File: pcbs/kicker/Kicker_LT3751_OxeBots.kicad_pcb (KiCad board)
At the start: 2 copper layers, 117.9 x 140 mm, 91 parts, among them J1 XT30PW-F, J2 Conn_01x02, J3 Conn_01x02, J4 Conn_01x08, J5 XT30PW-F, Q1 BC847, Q2 BC847, Q3 IRFB4227, Q4 TIC106, Q5 FQPF20N60, T1 DCT15EFD-U44S003, U1 LM324, U2 LMV358, U3 TLV431DBZ, U4 LT3751, U5 AQV454, U6 HCNR201, U7 HCPL-3120, U8 LM358

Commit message: Desenhada versão inicial da PCB.
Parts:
- removed C6: 100nF, Capacitor_SMD:C_0805_2012Metric_Pad1.18x1.45mm_HandSolder
- removed R13, R8, R9: 10k, Resistor_SMD:R_0805_2012Metric_Pad1.20x1.40mm_HandSolder
- removed R27: 5.6k, Resistor_SMD:R_0805_2012Metric_Pad1.20x1.40mm_HandSolder
- removed R28, R5: 1k, Resistor_SMD:R_0805_2012Metric_Pad1.20x1.40mm_HandSolder
- removed U2: LMV358, Package_SO:SOIC-8_5.3x6.2mm_P1.27mm
- C8: footprint Capacitor_THT:C_Disc_D5.0mm_W2.5mm_P2.50mm -> Capacitor_SMD:C_0805_2012Metric_Pad1.18x1.45mm_HandSolder
- D4, R7: moved to B.Cu
- R34: footprint Resistor_THT:R_Axial_DIN0207_L6.3mm_D2.5mm_P7.62mm_Horizontal -> Resistor_THT:R_Axial_DIN0207_L6.3mm_D2.5mm_P15.24mm_Horizontal
- R42: footprint Resistor_THT:R_Axial_DIN0207_L6.3mm_D2.5mm_P15.24mm_Horizontal -> Resistor_THT:R_Axial_DIN0207_L6.3mm_D2.5mm_P7.62mm_Horizontal
- moved R22 19.8 mm to (78.3, 64.0), turned to 135 degrees
- moved R17 18.4 mm to (79.2, 68.1), turned to -135 degrees
- moved R21 18.2 mm to (72.8, 70.2), turned to 135 degrees
- moved F1 16.1 mm to (72.1, 100.7), turned to -90 degrees
- moved Q2 13.9 mm to (75.4, 66.9), turned to 135 degrees
- moved R16 13.7 mm to (73.8, 74.0), turned to -135 degrees
- moved C3 13.3 mm to (81.2, 88.0), turned to -90 degrees
- moved D4 12.8 mm to (79.3, 112.1), turned to 0 degrees
- moved R42 12.7 mm to (132.7, 61.0)
- moved R11 9.81 mm to (46.6, 124.9), turned to 0 degrees
- moved R12 9.81 mm to (64.5, 77.6), turned to -90 degrees
- moved Q1 9.29 mm to (69.6, 72.7), turned to 135 degrees
- moved R34 9.04 mm to (119.3, 134.1), turned to 90 degrees
- moved R37 7.64 mm to (117.9, 143.4), turned to 180 degrees
- moved R24 6.97 mm to (56.8, 108.0), turned to 180 degrees
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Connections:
- C9 pad 1: Net-(U1C--) -> Net-(U1D--)
- C9 pad 2: Net-(U1B-+) -> Net-(U1C-+)
- J4 pad 3: EXT_OUT_FB -> EXT_OUT_LT3751_FAULT
- J4 pad 4: EXT_OUT_LT3751_FAULT -> EXT_OUT_LT3751_DONE
- J4 pad 5: EXT_OUT_LT3751_DONE -> EXT_OUT_FB
- R12 pad 1: Net-(U2A-+) -> EXT_OUT_FB
- R12 pad 2: Net-(U1D--) -> Net-(U1A--)
- R14 pad 2: Net-(U1A--) -> Net-(U1B--)
- R23 pad 1: Net-(U1B--) -> Net-(U1C--)
- R23 pad 2: Net-(U1A-+) -> Net-(U1B-+)
- R25 pad 1: Net-(U1B--) -> Net-(U1C--)
- R25 pad 2: Net-(U1D-+) -> Net-(U1A-+)
- R26 pad 1: Net-(U1D-+) -> Net-(U1A-+)
- R31 pad 2: Net-(U1C--) -> Net-(U1D--)
- R41 pad 1: Net-(U8A--) -> Net-(U8B--)
- R41 pad 2: Net-(U8B--) -> Net-(U8A--)
- R44 pad 2: Net-(U8B-+) -> Net-(U8A-+)
- R45 pad 1: Net-(U8B-+) -> Net-(U8A-+)
- RV1 pad 1: Net-(U1A-+) -> Net-(U1B-+)
- RV2 pad 2: Net-(U1B-+) -> Net-(U1C-+)
- RV2 pad 3: Net-(U1B-+) -> Net-(U1C-+)
- U1 pad 10: GND -> Net-(U1C-+)
- U1 pad 12: Net-(U1D-+) -> GND
- U1 pad 14: Net-(U1D--) -> Net-(U1C-+)
- U1 pad 8: Net-(U1B-+) -> Net-(U1C--)
- U6 pad 3: Net-(U8A--) -> Net-(U8B--)
- U6 pad 6: Net-(U1C--) -> Net-(U1D--)
- U8 pad 1: Net-(R36-Pad2) -> Net-(U8A--)
- U8 pad 3: GNDPWR -> Net-(U8A-+)
- U8 pad 5: Net-(U8B-+) -> GNDPWR
- U8 pad 7: Net-(U8B--) -> Net-(R36-Pad2)
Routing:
- net +12V: track 33.7 -> 175.0 mm, vias 0 -> 3
- net EXT_IN_LT3751_ENABLE: track 1.21 -> 53.8 mm
- net Net-(U1D--): track 15.0 -> 61.4 mm
- net LT3751_FAULT: track 48.2 -> 84.1 mm, vias 0 -> 1
- net Net-(Q3-G): track 0.00 -> 29.0 mm
- net LT3751_DONE: track 49.3 -> 75.8 mm, vias 0 -> 1
- net Net-(U1C-+): track 0.00 -> 22.2 mm, vias 0 -> 2
- net Net-(U1A--): track 7.87 -> 29.9 mm, vias 1 -> 2
- net EXT_IN_LT3751_KICK_1: track 13.5 -> 34.6 mm
- net GNDPWR: track 20.7 -> 0.00 mm, vias 0 -> 37
- net Net-(R5-Pad2): track 19.9 -> 0.00 mm
- net Net-(Q3-S): track 0.08 -> 18.5 mm, vias 0 -> 2
- net Net-(U8A-+): track 0.00 -> 18.4 mm
- net Net-(U2A-+): track 18.1 -> 0.00 mm, vias 2 -> 0
- net Net-(Q3-D): track 0.03 -> 17.0 mm
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- added copper zone on B.Cu, net +24V
- added copper zone on F.Cu, net +24V
- added copper zone on B.Cu, net GND
- added copper zone on F.Cu, net GND
- added copper zone on B.Cu, net Net-(F1-Pad1)

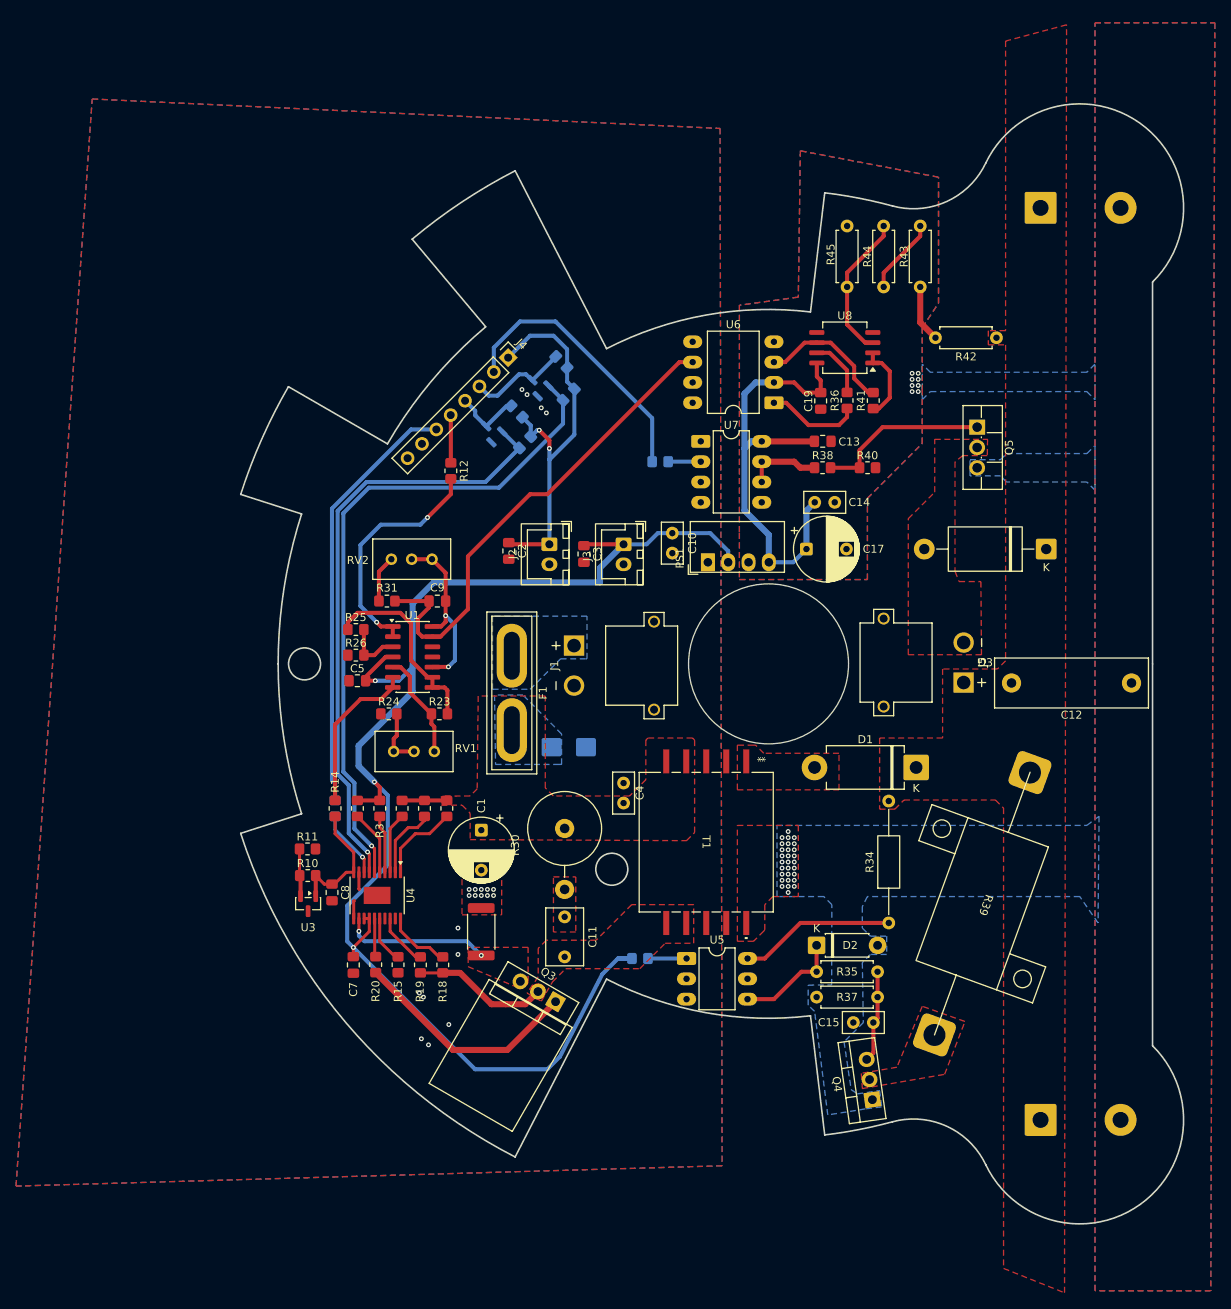
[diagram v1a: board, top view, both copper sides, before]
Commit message: Revisados os furos e adicionado MCU STM32
* Adicionado MCU STM32
* Corrigida posição dos furos
* Invertida a posição dos capacitores
* Realizadas melhorias na em geral
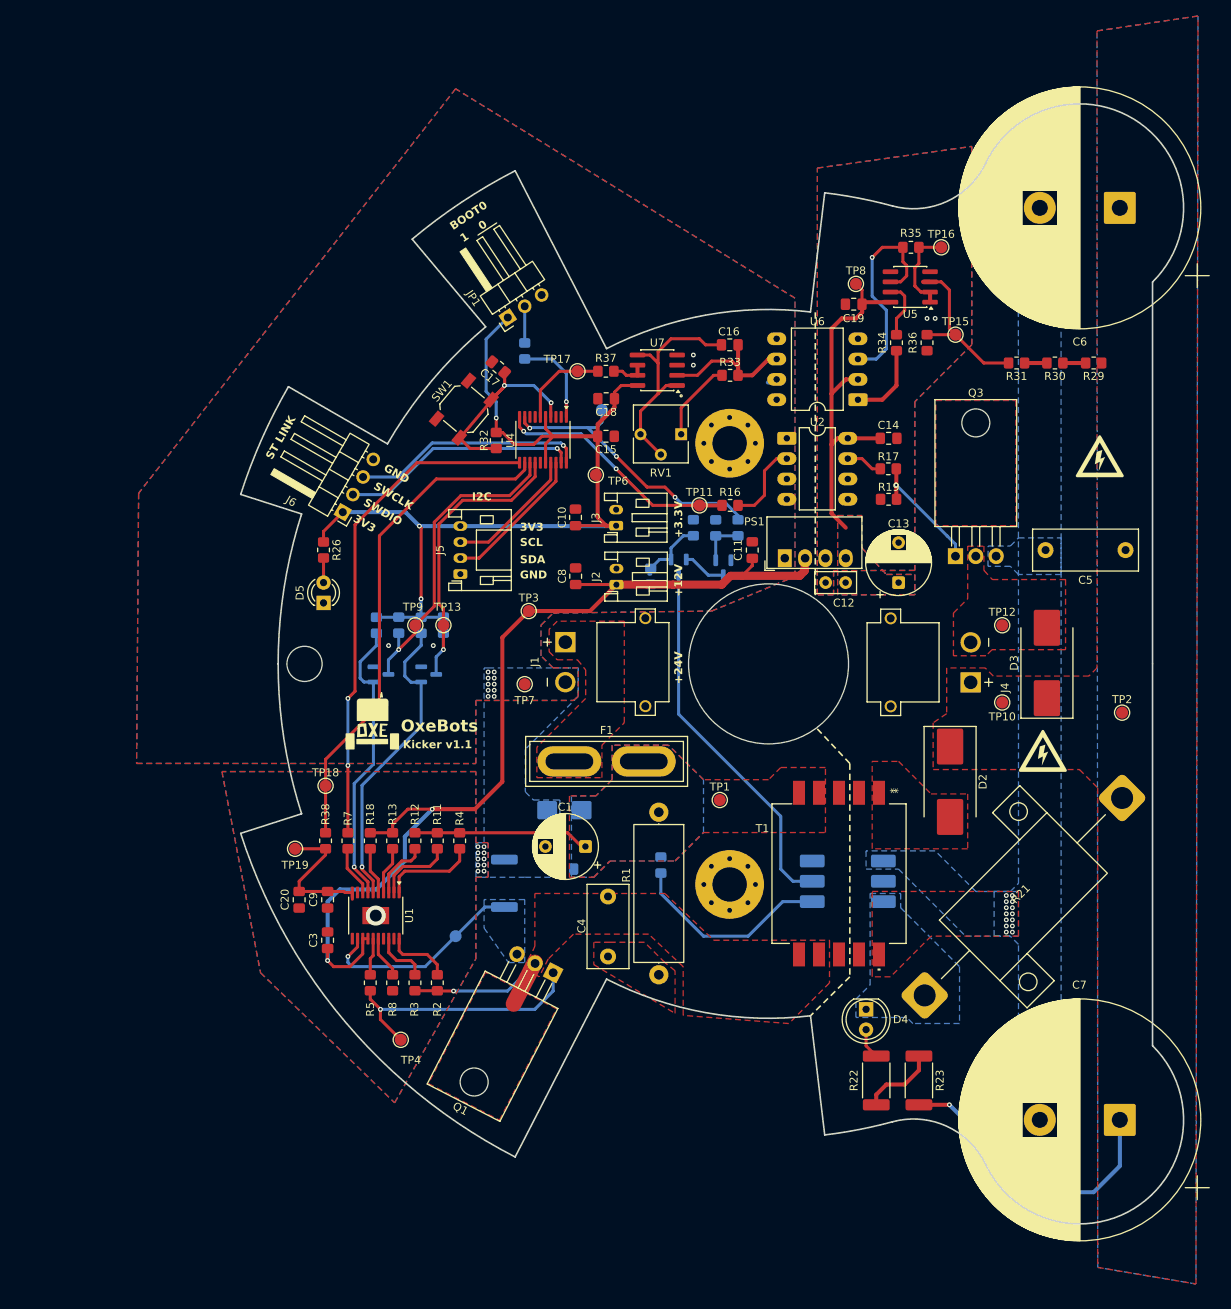
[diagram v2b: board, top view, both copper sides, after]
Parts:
- removed the C11 at (78.7, 133.3)
- removed the C5 at (52.8, 103.8)
- removed the C8 at (49.7, 130.3)
- removed the D1 at (122.7, 114.7)
- removed the J4 at (71.7, 63.4)
- removed the Q1 at (69.6, 72.7)
- removed the R11 at (46.6, 124.9)
- removed the R12 at (64.5, 77.6)
- removed the R16 at (73.8, 74.0)
- removed the R17 at (79.2, 68.1)
- removed the R31 at (56.5, 93.9)
- removed the R34 at (119.3, 134.1)
- removed the R35 at (110.2, 140.2)
- removed RV2: 100k, Potentiometer_THT:Potentiometer_Bourns_3296W_Vertical
- removed the U1 at (59.7, 100.9)
- removed the U3 at (46.7, 131.7)
- added C16: 1nF, Capacitor_SMD:C_0805_2012Metric_Pad1.18x1.45mm_HandSolder, F.Cu at (99.4, 61.8)
- added C17: 100nF, Capacitor_SMD:C_0805_2012Metric_Pad1.18x1.45mm_HandSolder, F.Cu at (70.4, 64.6)
- added C18: 100nF, Capacitor_SMD:C_0805_2012Metric_Pad1.18x1.45mm_HandSolder, F.Cu at (83.9, 68.6)
- added C20: 100nF, Capacitor_SMD:C_0805_2012Metric_Pad1.18x1.45mm_HandSolder, F.Cu at (45.6, 131.2)
- added C4: 2.2nF, Capacitor_THT:C_Rect_L10.3mm_W5.0mm_P7.50mm_MKS4, F.Cu at (84.2, 138.3)
- added D4: LED, LED_THT:LED_D5.0mm, F.Cu at (116.4, 144.9)
- added D5: LED, LED_THT:LED_D3.0mm, F.Cu at (48.6, 94.1)
- added G***: LOGO, oxebots:Logo_OxeBots_10mm, F.Cu at (54.6, 109.3)
- added G***: LOGO, oxebots:Icon_High_Voltage_10mm, F.Cu at (145.6, 76.1)
- added G***: LOGO, oxebots:Icon_High_Voltage_10mm, F.Cu at (138.5, 112.9)
- added G***: LOGO, oxebots:Icon_High_Voltage_10mm, B.Cu at (124.8, 114.9)
- added H1: MountingHole, MountingHole:MountingHole_4.3mm_M4_Pad_Via, F.Cu at (99.4, 74.2)
- added H2: MountingHole, MountingHole:MountingHole_4.3mm_M4_Pad_Via, F.Cu at (99.4, 129.3)
- added J5: I2C, Connector_JST:JST_PH_S4B-PH-K_1x04_P2.00mm_Horizontal, F.Cu at (65.7, 90.5)
- added J6: ST Link, Connector_PinHeader_2.54mm:PinHeader_1x04_P2.54mm_Horizontal, F.Cu at (51.0, 82.8)
- added JP1: Boot0, Connector_PinHeader_2.54mm:PinHeader_1x03_P2.54mm_Horizontal, F.Cu at (71.6, 58.4)
- added Q5: BSS138, Package_TO_SOT_SMD:SOT-23, B.Cu at (93.0, 89.6)
- added Q6: BSS138, Package_TO_SOT_SMD:SOT-23, B.Cu at (98.6, 89.7)
- added R15: 1k, Resistor_SMD:R_0805_2012Metric_Pad1.20x1.40mm_HandSolder, B.Cu at (63.6, 96.9)
- added R27: 10R, Resistor_SMD:R_0805_2012Metric_Pad1.20x1.40mm_HandSolder, B.Cu at (100.4, 84.7)
- added R28: 10k, Resistor_SMD:R_0805_2012Metric_Pad1.20x1.40mm_HandSolder, B.Cu at (97.6, 84.7)
- added R32: 10k, Resistor_SMD:R_0805_2012Metric_Pad1.20x1.40mm_HandSolder, F.Cu at (70.2, 73.8)
- added R33: 47k, Resistor_SMD:R_0805_2012Metric_Pad1.20x1.40mm_HandSolder, F.Cu at (99.4, 65.7)
- added R38: 10k, Resistor_SMD:R_0805_2012Metric_Pad1.20x1.40mm_HandSolder, F.Cu at (48.9, 123.8)
- added R9: 10k, Resistor_SMD:R_0805_2012Metric_Pad1.20x1.40mm_HandSolder, B.Cu at (55.2, 96.9)
- added SW1: SW_Push, Button_Switch_SMD:SW_SPST_SKQG_WithStem, F.Cu at (66.1, 69.9)
- added TP1: +24V, TestPoint:TestPoint_Pad_D1.5mm, F.Cu at (98.1, 118.7)
- added TP10: SOL+, TestPoint:TestPoint_Pad_D1.5mm, F.Cu at (133.4, 106.6)
- added TP11: KICK_PWM, TestPoint:TestPoint_Pad_D1.5mm, F.Cu at (95.6, 81.9)
- added TP12: SOL-, TestPoint:TestPoint_Pad_D1.5mm, F.Cu at (133.4, 96.9)
- added TP13: FAULT, TestPoint:TestPoint_Pad_D1.5mm, F.Cu at (63.6, 96.9)
- added TP14: BLEEDER, TestPoint:TestPoint_Pad_D1.5mm, B.Cu at (83.4, 70.0)
- added TP15: VD_SEC, TestPoint:TestPoint_Pad_D1.5mm, F.Cu at (127.6, 60.6)
- added TP16: VD_SEC_BUFFER, TestPoint:TestPoint_Pad_D1.5mm, F.Cu at (125.8, 49.7)
- added TP17: FB_ANALOG, TestPoint:TestPoint_Pad_D1.5mm, F.Cu at (80.4, 65.2)
- added TP18: FB_PWM, TestPoint:TestPoint_Pad_D1.5mm, F.Cu at (48.9, 117.0)
- added TP19: FB_ANALOG, TestPoint:TestPoint_Pad_D1.5mm, F.Cu at (45.0, 124.8)
- added TP2: VCAP, TestPoint:TestPoint_Pad_D1.5mm, F.Cu at (148.4, 107.8)
- added TP3: +12V, TestPoint:TestPoint_Pad_D1.5mm, F.Cu at (74.3, 95.1)
- added TP4: HVGATE, TestPoint:TestPoint_Pad_D1.5mm, F.Cu at (58.3, 148.7)
- added TP5: CSP, TestPoint:TestPoint_Pad_D1.5mm, B.Cu at (65.1, 135.8)
- added TP6: +3.3V, TestPoint:TestPoint_Pad_D1.5mm, F.Cu at (82.6, 78.1)
- added TP7: GND, TestPoint:TestPoint_Pad_D1.5mm, F.Cu at (73.7, 104.3)
- added TP8: +15V_SEC, TestPoint:TestPoint_Pad_D1.5mm, F.Cu at (115.2, 54.2)
- added TP9: DONE, TestPoint:TestPoint_Pad_D1.5mm, F.Cu at (60.1, 96.9)
- added U4: STM32F070F6Px, Package_SO:TSSOP-20_4.4x6.5mm_P0.65mm, F.Cu at (76.0, 73.7)
- added U7: TLV9002, Package_SO:SOIC-8_3.9x4.9mm_P1.27mm, F.Cu at (90.3, 65.0)
- C11: renamed from C10; footprint Capacitor_THT:C_Disc_D5.0mm_W2.5mm_P2.50mm -> Capacitor_SMD:C_0805_2012Metric_Pad1.18x1.45mm_HandSolder
- C15: footprint Capacitor_THT:C_Disc_D5.0mm_W2.5mm_P2.50mm -> Capacitor_SMD:C_0805_2012Metric_Pad1.18x1.45mm_HandSolder
- C2: renamed from C4; footprint Capacitor_THT:C_Disc_D5.0mm_W2.5mm_P2.50mm -> Capacitor_SMD:C_0805_2012Metric_Pad1.18x1.45mm_HandSolder; moved to B.Cu
- C5: renamed from C12; footprint Capacitor_THT:C_Rect_L19.0mm_W6.0mm_P15.00mm_MKS4 -> Capacitor_THT:C_Rect_L13.0mm_W5.0mm_P10.00mm_FKS3_FKP3_MKS4
- C6: renamed from C16; moved to F.Cu
- C7: renamed from C18; moved to F.Cu
- C9: value 1nF -> 10nF
- D2: value 1N4712A -> MURS460; footprint Diode_THT:D_DO-41_SOD81_P7.62mm_Horizontal -> Diode_SMD:D_SMC_Handsoldering
- D3: value 1.5KE220A -> MURS460; footprint Diode_THT:D_DO-201AE_P15.24mm_Horizontal -> Diode_SMD:D_SMC_Handsoldering
- F1: value Fuse -> 10A
- J1: footprint oxebots_connectors:AMASS_XT30PW-M -> oxebots:AMASS_XT30PW-M
- J2: renamed from J3; value Conn_01x02 -> 12V; footprint Connector_JST:JST_XH_B2B-XH-A_1x02_P2.50mm_Vertical -> Connector_JST:JST_PH_S2B-PH-K_1x02_P2.00mm_Horizontal
- J3: renamed from J2; value Conn_01x02 -> 3.3V; footprint Connector_JST:JST_XH_B2B-XH-A_1x02_P2.50mm_Vertical -> Connector_JST:JST_PH_S2B-PH-K_1x02_P2.00mm_Horizontal
- J4: renamed from J5; footprint oxebots_connectors:AMASS_XT30PW-M -> oxebots:AMASS_XT30PW-M
- PS1: footprint Converter_DCDC:Converter_DCDC_Murata_MEE1SxxxxSC_THT -> oxebots:DC-DC_Converter_BxxxxS_1W
- Q1: renamed from Q3; footprint Package_TO_SOT_THT:TO-220-3_Vertical -> Package_TO_SOT_THT:TO-220-3_Horizontal_TabDown
- Q3: renamed from Q5; footprint Package_TO_SOT_THT:TO-220F-3_Vertical -> Package_TO_SOT_THT:TO-220-3_Horizontal_TabDown
- Q4: value TIC106 -> BC847; footprint Package_TO_SOT_THT:TO-220-3_Vertical -> Package_TO_SOT_SMD:SOT-23; moved to B.Cu
- R1: renamed from R30; footprint Resistor_THT:R_Axial_DIN0922_L20.0mm_D9.0mm_P7.62mm_Vertical -> Resistor_THT:R_Axial_DIN0617_L17.0mm_D6.0mm_P20.32mm_Horizontal
- R10: value 1.2k -> 1k; moved to B.Cu
- R14: value 1k -> 10k; moved to B.Cu
- R16: renamed from R33; value 220R -> 150R; moved to F.Cu
- R20: renamed from R32; value 1k -> 2.7k
- R21: value 4.7k -> 2.7k 25W; footprint Resistor_SMD:R_0805_2012Metric_Pad1.20x1.40mm_HandSolder -> oxebots:Resistor_RX24_10W; moved to F.Cu
- R22: value 4.7k -> 12k 2W; footprint Resistor_SMD:R_0805_2012Metric_Pad1.20x1.40mm_HandSolder -> Resistor_SMD:R_2512_6332Metric_Pad1.40x3.35mm_HandSolder; moved to F.Cu
- R23: value 1k -> 12k 2W; footprint Resistor_SMD:R_0805_2012Metric_Pad1.20x1.40mm_HandSolder -> Resistor_SMD:R_2512_6332Metric_Pad1.40x3.35mm_HandSolder
- R24: value 330R -> 10R; moved to B.Cu
- R25: value 20k -> 10k; moved to B.Cu
- R26: value 10k -> 150R
- R29: renamed from R42; value 510k -> 330k; footprint Resistor_THT:R_Axial_DIN0207_L6.3mm_D2.5mm_P7.62mm_Horizontal -> Resistor_SMD:R_0805_2012Metric_Pad1.20x1.40mm_HandSolder
- R30: renamed from R43; value 510k -> 330k; footprint Resistor_THT:R_Axial_DIN0207_L6.3mm_D2.5mm_P7.62mm_Horizontal -> Resistor_SMD:R_0805_2012Metric_Pad1.20x1.40mm_HandSolder
- R31: renamed from R44; value 47k -> 330k; footprint Resistor_THT:R_Axial_DIN0207_L6.3mm_D2.5mm_P7.62mm_Horizontal -> Resistor_SMD:R_0805_2012Metric_Pad1.20x1.40mm_HandSolder
- R35: renamed from R41; value 330k -> 56k
- R36: renamed from R45; value 33k -> 10k; footprint Resistor_THT:R_Axial_DIN0207_L6.3mm_D2.5mm_P7.62mm_Horizontal -> Resistor_SMD:R_0805_2012Metric_Pad1.20x1.40mm_HandSolder
- R37: value 100k -> 1k; footprint Resistor_THT:R_Axial_DIN0207_L6.3mm_D2.5mm_P7.62mm_Horizontal -> Resistor_SMD:R_0805_2012Metric_Pad1.20x1.40mm_HandSolder
- R39: value 1k -> 10k; footprint oxebots:Resistor_RX24_10W -> Resistor_SMD:R_0805_2012Metric_Pad1.20x1.40mm_HandSolder; moved to B.Cu
- R6: renamed from R29; moved to B.Cu
- R7: value 220R -> 1k; moved to F.Cu
- R8: renamed from R15; value 1,5K -> 1,8K
- RV1: value 100k -> 20k; footprint Potentiometer_THT:Potentiometer_Bourns_3296W_Vertical -> oxebots:trimpot_3362P
- T1: footprint oxebots_transformer:TRANS_U44S003_TDK -> oxebots:TRANS_U44S003_TDK
- U3: renamed from U5; footprint Package_DIP:DIP-6_W7.62mm_LongPads -> Package_DIP:DIP-6_W8.89mm_SMDSocket_LongPads; moved to B.Cu
- U5: renamed from U8; footprint Package_SO:SOIC-8_5.3x6.2mm_P1.27mm -> Package_SO:SOIC-8_3.9x4.9mm_P1.27mm
- moved R22 98.0 mm to (117.7, 153.8), turned to -90 degrees
- moved R39 89.7 mm to (73.7, 62.6), turned to -90 degrees
- moved R21 87.7 mm to (136.1, 130.8), turned to 45 degrees
- moved R37 85.3 mm to (83.9, 65.2), turned to 0 degrees
- moved C15 80.5 mm to (83.9, 73.3), turned to 0 degrees
- moved Q4 76.8 mm to (61.7, 103.0), turned to 0 degrees
- moved R23 75.4 mm to (123.0, 153.8), turned to -90 degrees
- moved RV1 50.2 mm to (93.3, 73.0), turned to 180 degrees
- moved R25 44.1 mm to (94.8, 84.7), turned to 90 degrees
- moved Q2 41.1 mm to (55.8, 103.0), turned to 0 degrees
- moved C9 39.8 mm to (49.1, 131.2), turned to -90 degrees
- moved R24 37.0 mm to (89.5, 90.8), turned to 90 degrees
- moved R10 33.3 mm to (58.0, 96.9), turned to -90 degrees
- moved D2 26.4 mm to (126.9, 116.5), turned to -90 degrees
- moved R14 25.3 mm to (60.8, 96.9), turned to -90 degrees
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- renumbered C2 to C10, C14 to C12, C17 to C13, C13 to C14, C7 to C3, C3 to C8, D4 to D1, R1 to R11, R2 to R12, R3 to R13, R38 to R17, R4 to R18, R40 to R19, R18 to R2, R19 to R3, R36 to R34, R6 to R4, R20 to R5, U4 to U1, U7 to U2
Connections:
- C15 pad 1: Net-(Q4-G) -> +3.3V
- C15 pad 2: GNDPWR -> GND
- C9 pad 1: Net-(U1D--) -> LT3751_FB
- C9 pad 2: Net-(U1C-+) -> GND
- D2 pad 1: Net-(D2-K) -> VCAP
- D2 pad 2: GNDPWR -> Net-(D2-A)
- Q2 pad 1: LT3751_FAULT -> LT3751_DONE
- Q2 pad 3: EXT_OUT_LT3751_FAULT -> MCU_IN_DONE
- Q4 pad 1: GNDPWR -> LT3751_FAULT
- Q4 pad 2: Net-(Q4-A) -> GND
- Q4 pad 3: Net-(Q4-G) -> MCU_IN_FAULT
- R10 pad 1: LT3751_FB -> +3.3V
- R10 pad 2: Net-(U3-REF) -> MCU_IN_DONE
- R14 pad 1: LT3751_FB -> +3.3V
- R14 pad 2: Net-(U1B--) -> LT3751_FAULT
- R16 pad 1: EXT_IN_LT3751_KICK_1 -> MCU_PWM_OUT_KICK
- R17 pad 1: Net-(R38-Pad1) -> Net-(R17-Pad1)
- R20 pad 1: +12V -> +24V
- R21 pad 1: +3.3V -> Net-(D4-K)
- R21 pad 2: EXT_OUT_LT3751_DONE -> VCAP
- R22 pad 1: +3.3V -> Net-(D4-A)
- R22 pad 2: EXT_OUT_LT3751_FAULT -> Net-(R22-Pad2)
- R23 pad 1: Net-(U1C--) -> Net-(R22-Pad2)
- R23 pad 2: Net-(U1B-+) -> VCAP
- R24 pad 1: Net-(R24-Pad1) -> +12V
- R24 pad 2: GND -> Net-(Q5-G)
- R25 pad 1: Net-(U1C--) -> Net-(Q5-G)
- R25 pad 2: Net-(U1A-+) -> GND
- R26 pad 1: Net-(U1A-+) -> +3.3V
- R26 pad 2: GND -> Net-(D5-A)
- R37 pad 1: Net-(Q4-G) -> MCU_ADC_IN_FB
- R37 pad 2: GNDPWR -> Net-(U7B--)
- R39 pad 1: VCAP -> Net-(JP1-C)
- R39 pad 2: Net-(Q4-A) -> MCU_BOOT0
- R7 pad 1: EXT_IN_LT3751_ENABLE -> MCU_OUT_ENABLE
- RV1 pad 1: Net-(U1B-+) -> Net-(R33-Pad1)
- RV1 pad 2: Net-(R24-Pad1) -> Net-(U7B-+)
- RV1 pad 3: Net-(R24-Pad1) -> Net-(U7B-+)
- T1 pad 1: Net-(D1-A) -> Net-(D2-A)
- U2 pad 6: Net-(R38-Pad1) -> unconnected-(U2-VO-Pad6)
- U2 pad 7: Net-(R38-Pad1) -> Net-(R17-Pad1)
- U3 pad 2: GND -> Net-(Q5-D)
- U3 pad 4: Net-(D2-K) -> GNDPWR
- U3 pad 6: Net-(R34-Pad1) (its old number) -> Net-(D4-K)
- U6 pad 6: Net-(U1D--) -> Net-(U7A--)
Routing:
- net +3.3V: track 48.9 -> 124.4 mm, vias 2 -> 3
- net MCU_OUT_ENABLE: track 0.00 -> 62.7 mm, vias 0 -> 2
- net MCU_PWM_OUT_FB: track 0.00 -> 62.4 mm
- net Net-(U1D--): track 61.4 -> 0.00 mm
- net EXT_IN_LT3751_ENABLE: track 53.8 -> 0.00 mm
- net Net-(Q5-D): track 0.00 -> 46.2 mm
- net +12V: track 175.0 -> 129.1 mm, vias 3 -> 2
- net LT3751_FAULT: track 84.1 -> 38.5 mm
- net MCU_IN_DONE: track 0.00 -> 40.1 mm, vias 0 -> 1
- net LT3751_DONE: track 75.8 -> 36.3 mm
- net MCU_IN_FAULT: track 0.00 -> 37.7 mm, vias 0 -> 1
- net VCAP: track 0.00 -> 36.8 mm, vias 0 -> 1
- net MCU_OUT_BLEEDER: track 0.00 -> 36.4 mm, vias 0 -> 3
- net EXT_IN_LT3751_KICK_1: track 34.6 -> 0.00 mm
- net MCU_PWM_OUT_KICK: track 0.00 -> 30.6 mm, vias 0 -> 2
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- added copper zone on F.Cu, net (none)
- added copper zone on B.Cu, net +15V_SEC
- added copper zone on F.Cu, net +15V_SEC
- added copper zone on F.Cu, net Net-(D2-A)
- added copper zone on B.Cu, net Net-(D4-K)
- added copper zone on F.Cu, net Net-(F1-Pad1)
- added copper zone on B.Cu, net Net-(Q1-S)
- added copper zone on B.Cu, net VCAP
- removed copper zone on F.Cu, net Net-(D1-A)
- removed copper zone on B.Cu, net Net-(F1-Pad1)
- removed copper zone on F.Cu, net Net-(Q1-S)
- removed copper zone on F.Cu, net Net-(Q4-A)
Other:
- outline, holes or cut-outs redrawn
- board text added: "+12V"
- board text added: "+24V"
- board text added: "+3.3V"
- board text added: "0"
- board text added: "1"
- board text added: "3V3"
- board text added: "BOOT0"
- board text added: "Cuidado Alta Tensão"
- board text added: "GND"
- board text added: "I2C"
- board text added: "Kicker v1.1"
- board text added: "OxeBots"
- board text added: "SCL"
- board text added: "SDA"
- board text added: "ST LINK"
- board text added: "SWCLK"
- board text added: "SWDIO"

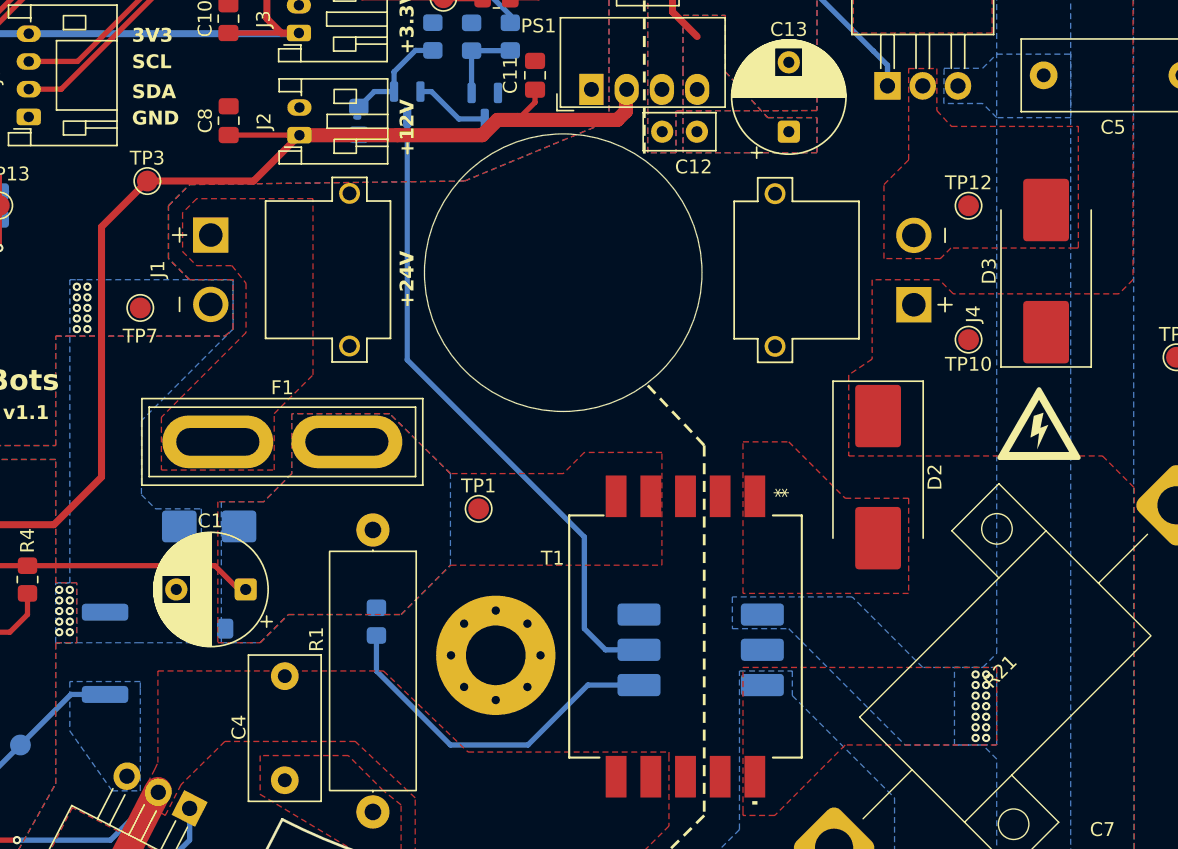
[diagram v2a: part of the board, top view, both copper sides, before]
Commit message: Ajustes no resistor do led do AQV454
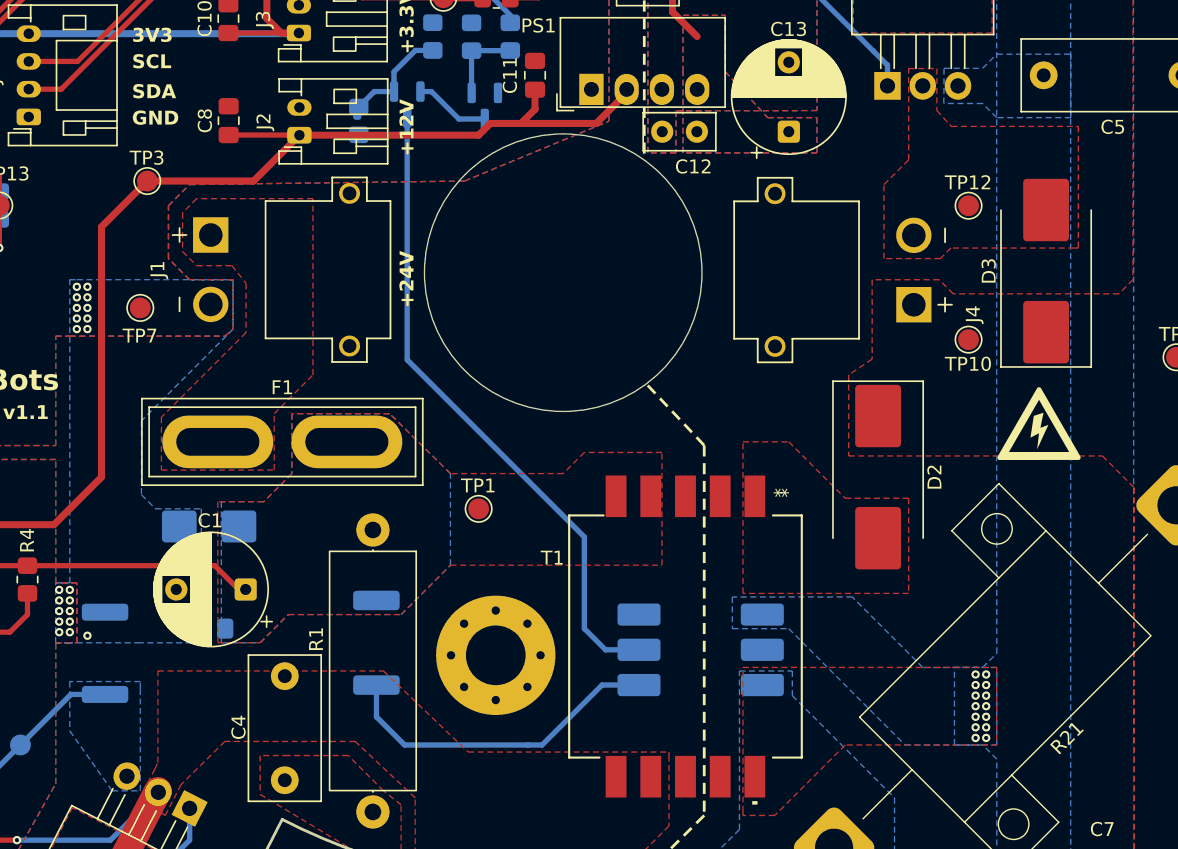
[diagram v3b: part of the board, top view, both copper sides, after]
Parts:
- R20: footprint Resistor_SMD:R_0805_2012Metric_Pad1.20x1.40mm_HandSolder -> Resistor_SMD:R_2512_6332Metric_Pad1.40x3.35mm_HandSolder
- R21: value 2.7k 25W -> 2.7k 10W
- moved R20 1.52 mm to (90.8, 128.4)
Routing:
- net Net-(R20-Pad2): track 25.0 -> 23.8 mm
- net +12V: track 129.1 -> 128.6 mm
- net GND: vias 25 -> 26
